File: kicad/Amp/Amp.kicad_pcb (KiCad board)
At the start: 2 copper layers, 30 x 25.6 mm, 23 parts, among them J1 Conn, J2 Conn, J3 Conn, J4 Conn, J5 Conn, J6 Conn, Q1 Q_NPN_BEC, U1 AD8541, U2 TS5A3166DBVR, U3 MCP1700

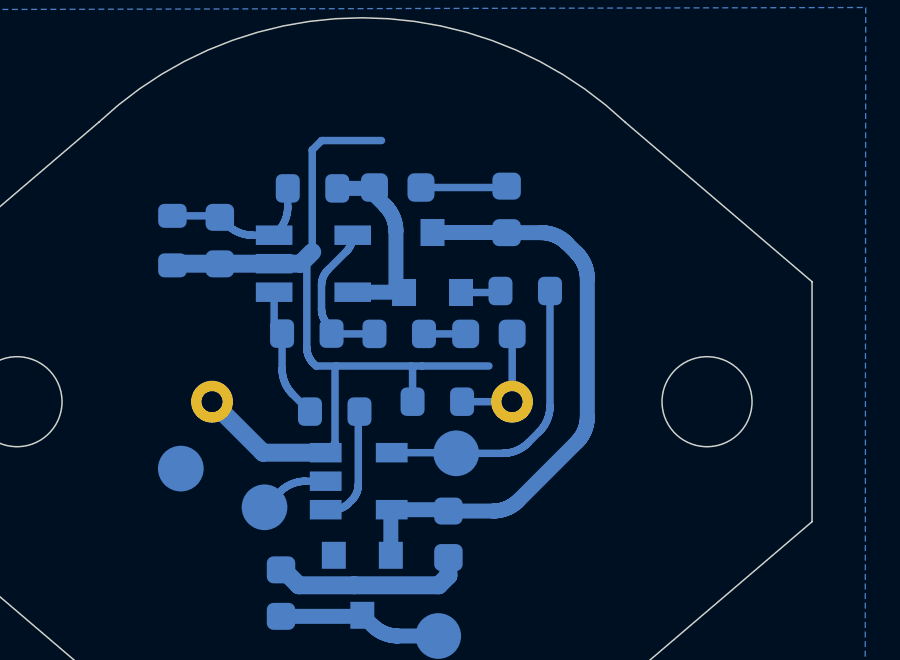
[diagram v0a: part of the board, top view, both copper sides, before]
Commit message: изменено:      kicad/Amp/Amp.kicad_pcb 	изменено:      kicad/Amp/Amp.kicad_pcb-bak
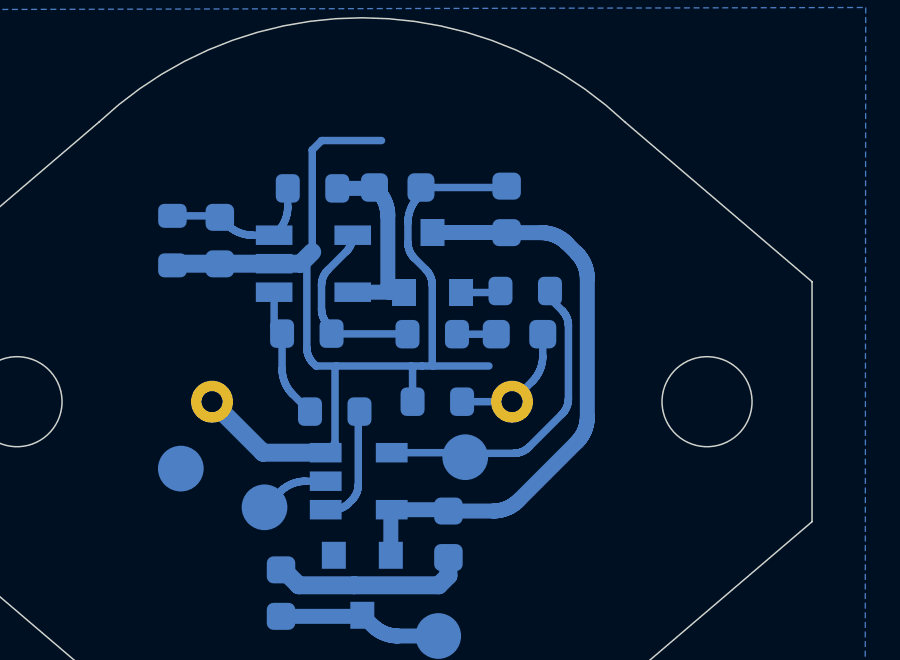
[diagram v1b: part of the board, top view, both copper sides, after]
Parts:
- moved R1 1.10 mm to (32.3, 55.3)
- moved C1 1.02 mm to (35.2, 55.3)
- moved J4 0.33 mm to (33.4, 59.4)
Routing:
- net GND: track 38.7 -> 45.0 mm
- net Net-(R1-Pad1): track 5.19 -> 6.31 mm
- net /Select: track 9.96 -> 10.6 mm

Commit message: изменено:      kicad/Amp/Amp-cache.lib 	изменено:      kicad/Amp/Amp.kicad_pcb 	изменено:      kicad/Amp/Amp.kicad_pcb-bak 	изменено:      kicad/Amp/Amp.sch 	изменено:      kicad/Amp/Amp.sch-bak 	изменено:      stm32cubeide/Anemometr_v3/Core/Src/main.c 	изменено:      stm32cubeide/Anemometr_v3/Core/Src/stm32f1xx_it.c 	изменено:      stm32cubeide/Anemometr_v3/Debug/Anemometr_3.bin 	изменено:      stm32cubeide/Anemometr_v3/Debug/Anemometr_3.elf 	изменено:      stm32cubeide/Anemometr_v3/Debug/Anemometr_3.list 	изменено:      stm32cubeide/Anemometr_v3/Debug/Anemometr_3.map 	изменено:      stm32cubeide/Anemometr_v3/Debug/Core/Src/main.o 	изменено:      stm32cubeide/Anemometr_v3/Debug/Core/Src/main.su 	изменено:      stm32cubeide/Anemometr_v3/Debug/Core/Src/stm32f1xx_it.o 	изменено:      stm32cubeide/Anemometr_v3/Release/Anemometr_3.bin 	изменено:      stm32cubeide/Anemometr_v3/Release/Anemometr_3.elf 	изменено:      stm32cubeide/Anemometr_v3/Release/Anemometr_3.list 	изменено:      stm32cubeide/Anemometr_v3/Release/Anemometr_3.map 	изменено:      stm32cubeide/Anemometr_v3/Release/Core/Src/main.o 	изменено:      stm32cubeide/Anemometr_v3/Release/Core/Src/main.su 	изменено:      stm32cubeide/Anemometr_v3/Release/Core/Src/stm32f1xx_it.o
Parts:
- added J7: Conn, My-library:SMD-CONN, B.Cu at (50.1, 80.3)
- added U4: TS5A3167DBVR, Package_TO_SOT_SMD:SOT-23-5, B.Cu at (46.5, 80.5)
- C1: footprint Capacitor_SMD:C_0603_1608Metric -> Resistor_SMD:R_0603_1608Metric
- J1, J2: footprint Connector_Pin:Pin_D0.7mm_L6.5mm_W1.8mm_FlatFork -> My-library:connBig
- moved R6 25.8 mm to (50.8, 75.8), turned to 270 degrees
- moved C3 24.5 mm to (38.4, 72.9)
- moved R3 24.5 mm to (36.8, 72.9)
- moved C5 23.9 mm to (47.8, 71.3)
- moved J6 23.9 mm to (37.0, 79.9)
- moved R2 23.9 mm to (41.4, 70.6)
- moved R4 23.9 mm to (41.2, 75.4)
- moved U1 23.9 mm to (41.4, 73.1)
- moved C2 23.9 mm to (44.2, 70.5)
- moved J1 23.9 mm to (48.0, 77.7)
- moved J2 23.9 mm to (38.0, 77.7)
- moved Q1 23.9 mm to (45.4, 73.0)
- moved R1 23.9 mm to (45.3, 75.4)
- moved U2 23.9 mm to (42.9, 80.3), turned to 270 degrees
- moved C6 23.9 mm to (44.3, 83.0), turned to 0 degrees
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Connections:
- net Net-(C5-Pad1) renamed /3.3v
- U2 pad 1: Net-(C4-Pad1) -> /Out
- U2 pad 2: /Out -> Net-(C4-Pad1)
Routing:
- net GND: track 45.0 -> 34.9 mm, vias 0 -> 2
- net /Select: track 10.6 -> 13.3 mm
- net /3.3v: track 20.1 -> 17.4 mm
- net /Signal: track 0.00 -> 2.49 mm
- net /In: track 4.29 -> 6.59 mm
- net Net-(C4-Pad1): track 4.00 -> 2.13 mm
- net Net-(C4-Pad2): track 4.42 -> 3.47 mm
- net /+5v: track 5.49 -> 4.90 mm
- added copper zone on F.Cu, net GND

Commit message: изменено:      kicad/Amp/Amp-cache.lib 	изменено:      kicad/Amp/Amp.kicad_pcb 	изменено:      kicad/Amp/Amp.kicad_pcb-bak 	изменено:      kicad/Amp/Amp.sch 	изменено:      kicad/Amp/Amp.sch-bak 	изменено:      kicad/Amp/fp-info-cache
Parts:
- removed J1, J2: Conn, My-library:connBig
- added L1: 47uH, Inductor_SMD:L_0805_2012Metric, B.Cu at (44.2, 85.1)
- added Z1: MCUSD18A40B12RS, My-library:MCUSD18A40B12RS, F.Cu at (43.0, 77.7)
- C3: value 1uF -> 10n
- R2, R3: value 100k -> 20k
- moved J3 3.38 mm to (46.9, 84.9)
- moved J5 1.08 mm to (39.1, 80.5)
- moved R5 0.23 mm to (48.4, 73.7)
- moved C5 0.14 mm to (47.7, 71.3)
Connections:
- C7 pad 1: /+5v -> Net-(C7-Pad1)
- U3 pad 3: /+5v -> Net-(C7-Pad1)
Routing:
- net GND: track 34.9 -> 50.5 mm
- net Net-(C7-Pad1): track 0.00 -> 4.51 mm
- net /+5v: track 4.90 -> 1.62 mm
- net /Out: track 2.25 -> 3.27 mm

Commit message: изменено:      kicad/Amp/Amp-cache.lib 	изменено:      kicad/Amp/Amp.kicad_pcb 	изменено:      kicad/Amp/Amp.kicad_pcb-bak 	изменено:      kicad/Amp/Amp.sch 	изменено:      kicad/Amp/Amp.sch-bak 	изменено:      kicad/Amp/fp-info-cache
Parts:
- removed Q1: Q_NPN_BEC, Package_TO_SOT_SMD:SOT-23
- removed the U1 at (41.4, 73.1)
- removed U4: TS5A3167DBVR, Package_TO_SOT_SMD:SOT-23-5
- added C1: 10uF, Capacitor_SMD:C_0603_1608Metric, B.Cu at (40.5, 85.2)
- added C6: 1.5n, Resistor_SMD:R_0402_1005Metric, B.Cu at (40.3, 80.6)
- added C7: 0.1uF, Capacitor_SMD:C_0402_1005Metric, B.Cu at (36.8, 79.4)
- added D1: MAX4477, Package_SO:MSOP-8_3x3mm_P0.65mm, B.Cu at (42.4, 79.7)
- added D2: TLV3501, Package_TO_SOT_SMD:SOT-23-6, B.Cu at (38.2, 82.9)
- added R1: 5.1k, Resistor_SMD:R_0402_1005Metric, B.Cu at (45.9, 74.6)
- added R7: 100k, Resistor_SMD:R_0402_1005Metric, B.Cu at (42.1, 83.4)
- added R8: 10k, Resistor_SMD:R_0402_1005Metric, B.Cu at (38.7, 80.4)
- added R9: 100k, Resistor_SMD:R_0402_1005Metric, B.Cu at (36.1, 82.4)
- C2: renamed from C1; footprint Resistor_SMD:R_0603_1608Metric -> Resistor_SMD:R_0402_1005Metric
- C3: value 10n -> 0.1uF; footprint Capacitor_SMD:C_0603_1608Metric -> Capacitor_SMD:C_0402_1005Metric
- C4: value 10n -> 100n; footprint Resistor_SMD:R_0603_1608Metric -> Resistor_SMD:R_0402_1005Metric
- R10: renamed from R5; value 10k -> 5.1k; footprint Resistor_SMD:R_0603_1608Metric -> Resistor_SMD:R_0402_1005Metric
- R2: renamed from R1; value 5.1k -> 1k; footprint Resistor_SMD:R_0603_1608Metric -> Resistor_SMD:R_0402_1005Metric
- R3: renamed from R2; value 20k -> 100k; footprint Resistor_SMD:R_0603_1608Metric -> Resistor_SMD:R_0402_1005Metric
- R4: renamed from R3; value 20k -> 100k; footprint Resistor_SMD:R_0603_1608Metric -> Resistor_SMD:R_0402_1005Metric
- R5: renamed from R4; footprint Resistor_SMD:R_0603_1608Metric -> Resistor_SMD:R_0402_1005Metric
- R6: footprint Resistor_SMD:R_0603_1608Metric -> Resistor_SMD:R_0402_1005Metric
- moved J5 17.2 mm to (36.2, 71.5)
- moved C5 16.5 mm to (36.0, 84.9), turned to 270 degrees
- moved L1 15.8 mm to (33.9, 73.1), turned to 90 degrees
- moved J4 14.4 mm to (44.2, 86.1)
- moved R10 13.4 mm to (36.8, 80.4)
- moved R3 13.1 mm to (44.1, 83.4)
- moved R6 10.9 mm to (40.2, 78.6), turned to 90 degrees
- moved C9 10.5 mm to (45.2, 81.5)
- moved C10 10.3 mm to (36.4, 74.2), turned to 0 degrees
- moved R4 9.85 mm to (45.0, 78.4), turned to 0 degrees
- moved C3 9.30 mm to (45.0, 79.4), turned to 0 degrees
- moved J3 7.58 mm to (40.2, 73.1)
- moved U2 7.48 mm to (33.6, 82.9), turned to 180 degrees
- moved U1 5.66 mm to (48.0, 82.7), turned to 180 degrees
- moved J2 5.32 mm to (38.7, 85.8), turned to 270 degrees
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- renumbered C7 to C10, C2 to C5, C6 to C8, C5 to C9, J7 to J1, J5 to J2, J6 to J3, J3 to J5, U2 to U1, U3 to U2
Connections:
- C2 pad 2: /In -> Net-(C2-Pad2)
- C5 pad 1: Net-(C2-Pad1) (its old number) -> /3.3v
- J1 pad 1: /Signal -> /Sig
- J4 pad 1: /Select -> /Sel
- R10 pad 1: /Select -> GND
- R3 pad 1: Net-(C2-Pad1) (its old number) -> /3.3v
- R6 pad 1: /In -> Net-(D1-Pad6)
- R6 pad 2: GND -> Net-(C4-Pad1)
- U1 pad 1: /Out -> Net-(C2-Pad2)
- U1 pad 2: Net-(C4-Pad1) -> /Sig
- U1 pad 4: /Select -> /Sel
- Z1 pad +: /In -> Net-(C2-Pad2)
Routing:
- net GND: track 50.5 -> 34.7 mm, vias 2 -> 4
- net /Sel: track 0.00 -> 13.6 mm
- net /Select: track 12.9 -> 0.00 mm
- net Net-(C2-Pad2): track 0.00 -> 8.15 mm
- net Net-(C2-Pad1) (its old number): track 6.61 -> 0.00 mm
- net /In: track 6.59 -> 0.00 mm
- net Net-(D1-Pad6): track 0.00 -> 6.36 mm
- net Net-(C10-Pad1): track 4.51 -> 10.9 mm
- net /3.3v: track 17.6 -> 23.8 mm
- net Net-(C6-Pad2): track 0.00 -> 4.90 mm
- net Net-(D1-Pad2): track 6.25 -> 2.88 mm
- net Net-(C3-Pad1): track 5.01 -> 8.35 mm
- net Net-(C6-Pad1): track 0.00 -> 2.52 mm
- net /Signal: track 2.49 -> 0.00 mm
- net Net-(C7-Pad1): track 1.37 -> 3.84 mm
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
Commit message: изменено:      kicad/Amp/Amp-cache.lib 	изменено:      kicad/Amp/Amp.kicad_pcb 	изменено:      kicad/Amp/Amp.kicad_pcb-bak 	изменено:      kicad/Amp/Amp.sch 	изменено:      kicad/Amp/Amp.sch-bak
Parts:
- C2, C4, C6: footprint Resistor_SMD:R_0402_1005Metric -> Capacitor_SMD:C_0402_1005Metric
- moved C6 0.07 mm to (40.3, 80.5)
- moved R6 0.06 mm to (40.3, 78.5)
- moved C4 0.06 mm to (40.3, 76.6)
- moved R4 0.05 mm to (45.0, 78.4)
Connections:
- net Net-(C2-Pad2) renamed /In

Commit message: изменено:      kicad/Amp/Amp-cache.lib 	изменено:      kicad/Amp/Amp.kicad_pcb 	изменено:      kicad/Amp/Amp.kicad_pcb-bak 	изменено:      kicad/Amp/Amp.sch 	изменено:      kicad/Amp/Amp.sch-bak
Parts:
- moved U2 12.7 mm to (38.5, 71.2), turned to 90 degrees
- moved C5 10.3 mm to (36.7, 74.6), turned to 0 degrees
- moved L1 7.81 mm to (40.6, 69.1)
- moved J5 7.81 mm to (42.9, 67.5)
- moved C10 7.78 mm to (43.1, 70.2)
- moved J3 1.58 mm to (41.8, 73.4)
- moved R10 1.04 mm to (37.7, 80.9)
- moved C7 1.04 mm to (37.7, 79.8)
- moved R8 0.50 mm to (39.2, 80.4), turned to 270 degrees
- moved D2 0.33 mm to (38.3, 83.2)
- moved R9 0.32 mm to (36.1, 82.7)
- moved J2 0.20 mm to (38.7, 86.0)
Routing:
- net /3.3v: track 23.8 -> 33.8 mm
- net Net-(C10-Pad1): track 10.9 -> 3.85 mm
- net GND: track 34.7 -> 32.2 mm

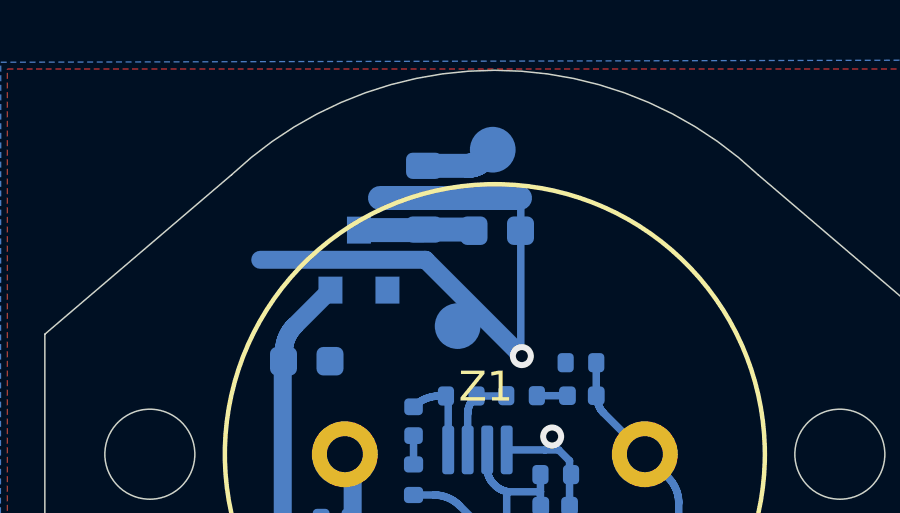
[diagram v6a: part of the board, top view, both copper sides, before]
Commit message: изменено:      kicad/Amp/Amp.kicad_pcb 	изменено:      kicad/Amp/Amp.kicad_pcb-bak
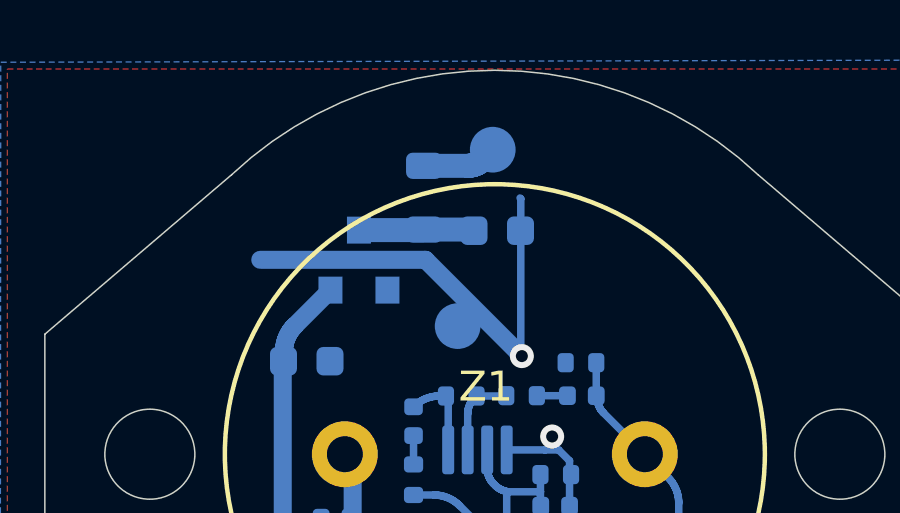
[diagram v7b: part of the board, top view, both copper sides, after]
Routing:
- net GND: track 32.2 -> 27.6 mm

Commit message: изменено:      kicad/Amp/Amp.kicad_pcb 	изменено:      kicad/Amp/Amp.kicad_pcb-bak 	изменено:      kicad/Amp/Amp.sch 	изменено:      kicad/Amp/Amp.sch-bak 	изменено:      stm32cubeide/Anemometr_v3/.mxproject 	изменено:      stm32cubeide/Anemometr_v3/Anemometr_3.ioc 	изменено:      stm32cubeide/Anemometr_v3/Core/Inc/main.h 	изменено:      stm32cubeide/Anemometr_v3/Core/Inc/stm32f1xx_hal_conf.h 	изменено:      stm32cubeide/Anemometr_v3/Core/Src/main.c 	изменено:      stm32cubeide/Anemometr_v3/Core/Src/stm32f1xx_it.c 	изменено:      stm32cubeide/Anemometr_v3/Debug/Anemometr_3.bin 	изменено:      stm32cubeide/Anemometr_v3/Debug/Anemometr_3.elf 	изменено:      stm32cubeide/Anemometr_v3/Debug/Anemometr_3.list 	изменено:      stm32cubeide/Anemometr_v3/Debug/Anemometr_3.map 	изменено:      stm32cubeide/Anemometr_v3/Debug/Core/Src/BME280.d 	изменено:      stm32cubeide/Anemometr_v3/Debug/Core/Src/BME280.o 	изменено:      stm32cubeide/Anemometr_v3/Debug/Core/Src/main.d 	изменено:      stm32cubeide/Anemometr_v3/Debug/Core/Src/main.o 	изменено:      stm32cubeide/Anemometr_v3/Debug/Core/Src/main.su 	изменено:      stm32cubeide/Anemometr_v3/Debug/Core/Src/stm32f1xx_hal_msp.d 	изменено:      stm32cubeide/Anemometr_v3/Debug/Core/Src/stm32f1xx_hal_msp.o 	изменено:      stm32cubeide/Anemometr_v3/Debug/Core/Src/stm32f1xx_it.d 	изменено:      stm32cubeide/Anemometr_v3/Debug/Core/Src/stm32f1xx_it.o 	изменено:      stm32cubeide/Anemometr_v3/Debug/Core/Src/stm32f1xx_it.su 	изменено:      stm32cubeide/Anemometr_v3/Debug/Core/Src/system_stm32f1xx.d 	изменено:      stm32cubeide/Anemometr_v3/Debug/Core/Src/system_stm32f1xx.o 	изменено:      stm32cubeide/Anemometr_v3/Debug/Drivers/STM32F1xx_HAL_Driver/Src/stm32f1xx_hal.d 	изменено:      stm32cubeide/Anemometr_v3/Debug/Drivers/STM32F1xx_HAL_Driver/Src/stm32f1xx_hal.o 	изменено:      stm32cubeide/Anemometr_v3/Debug/Drivers/STM32F1xx_HAL_Driver/Src/stm32f1xx_hal_cortex.d 	изменено:      stm32cubeide/Anemometr_v3/Debug/Drivers/STM32F1xx_HAL_Driver/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
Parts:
- R5: value 100k -> 390k
- moved C4 18.8 mm to (44.3, 58.2)
- moved C5 18.8 mm to (40.8, 56.2)
- moved C8 18.8 mm to (52.9, 66.6)
- moved D2 18.8 mm to (42.3, 64.8)
- moved R6 18.8 mm to (44.3, 60.1)
- moved R8 18.8 mm to (43.3, 62.0)
- moved R9 18.8 mm to (40.2, 64.3)
- moved C9 18.8 mm to (49.2, 63.0)
- moved J2 18.8 mm to (42.8, 67.6)
- moved J4 18.8 mm to (48.3, 67.7)
- moved J5 18.8 mm to (47.0, 49.1)
- moved R10 18.8 mm to (41.8, 62.5)
- moved R3 18.8 mm to (48.1, 65.0)
- moved R4 18.8 mm to (49.1, 60.0)
- moved R7 18.8 mm to (46.2, 65.0)
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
